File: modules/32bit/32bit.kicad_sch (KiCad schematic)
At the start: 62 parts, among them J5 USB_C_Receptacle_USB2.0_14P, SW1 K2-1808SN-A4SW-01, SW2 K2-1808SN-A4SW-01, SW4 K2-1808SN-A4SW-01, U1 ESP32-S3-WROOM-1U-N16R8, U3 MCP6002-xSN

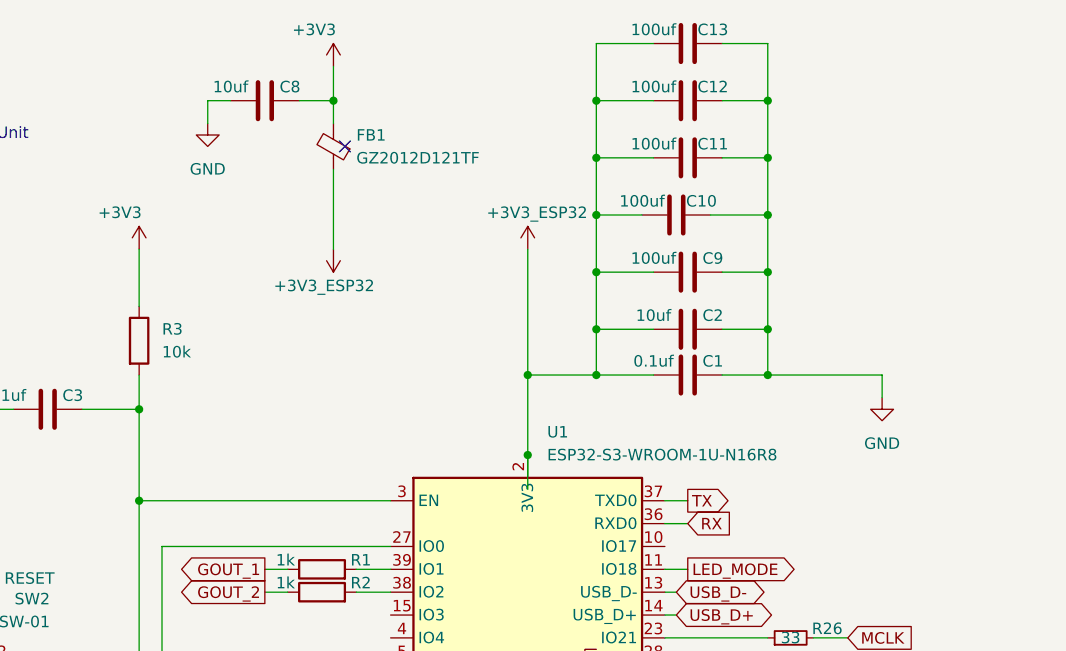
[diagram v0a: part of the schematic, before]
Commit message: Remove 32bit unwanted caps & etc
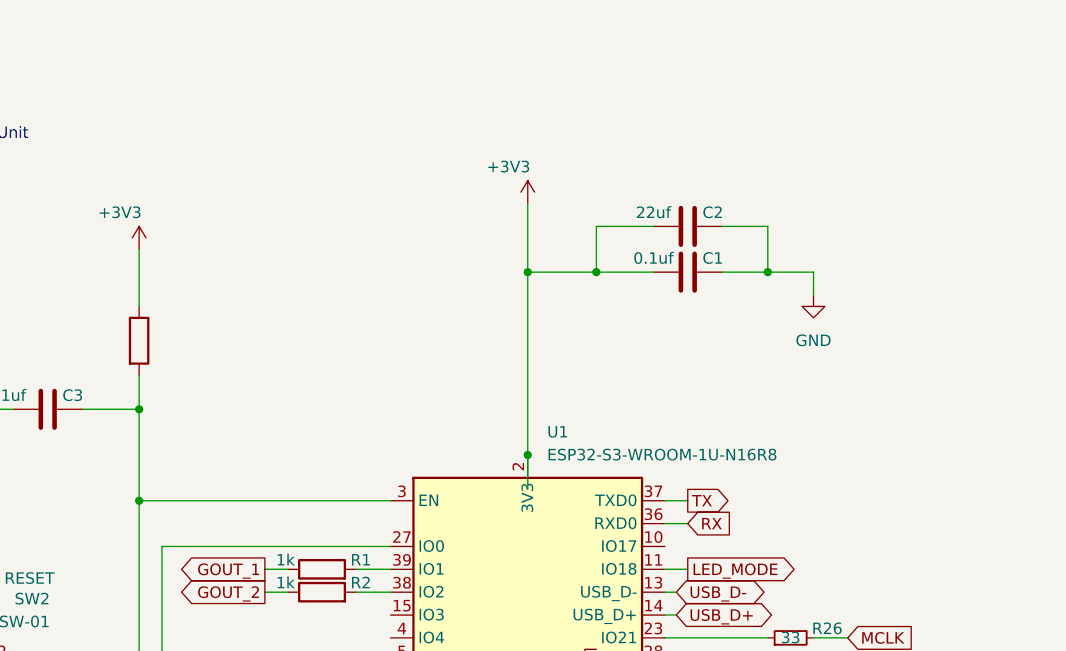
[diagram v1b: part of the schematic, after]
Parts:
- removed C10, C11, C12, C13, C9: 100uf, Capacitor_SMD:C_1206_3216Metric, symbol Device:C
- removed C8: 10uf, Capacitor_SMD:C_0603_1608Metric, symbol Device:C
- removed FB1: GZ2012D121TF, Capacitor_SMD:C_0805_2012Metric, symbol Device:FerriteBead_Small
- C2: value 10uf -> 22uf
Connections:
- net +3V3_ESP32 is gone; now on net +3V3: C1.1, C2.1, U1.2 (3V3)
- no-connect marks 1 -> 0
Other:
- moved on the sheet: C1, C2

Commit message: Add two LDO approach
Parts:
- removed C7: 100uf, Capacitor_SMD:C_1206_3216Metric, symbol Device:C_Small
- removed R15: 10, Resistor_SMD:R_0603_1608Metric, symbol Device:R_Small
- added C10, C7: 10uf, Capacitor_SMD:C_1206_3216Metric, symbol Device:C
- added C12: 100uf, Capacitor_SMD:C_1206_3216Metric, symbol Device:C
- added C17, C8: 22uf, Capacitor_SMD:C_1206_3216Metric, symbol Device:C
- added C9: 0.1uf, Capacitor_SMD:C_0402_1005Metric, symbol Device:C
- added FB1: GZ2012E800TF, Capacitor_SMD:C_0805_2012Metric, symbol Device:FerriteBead_Small
- added U5: AP2112K-3.3, Package_TO_SOT_SMD:SOT-23-5, symbol Regulator_Linear:AP2112K-3.3
- added U6: LP5907MFX-3.3, Package_TO_SOT_SMD:SOT-23-5, symbol Regulator_Linear:LP5907MFX-3.3
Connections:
- net +3V3: no longer C1.1, C2.1, C6.1, R10.1, R12.1, R3.1, U1.2 (3V3), U3.8 (V+)
- net +3V3_8388: no longer C21.1, C26.1, C37.1, C38.1, C39.1, C5.1, U4.16 (HPVDD), U4.17 (AVDD), U4.2 (DVDD)
- net GND: now also C17.2, C9.2
- net at J5.A4 (VBUS), J5.A9 (VBUS), J5.B4 (VBUS)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: now also C17.1, C9.1, FB1.1
- new net: C10.2, C7.2, U6.2 (GND)
- new net: C12.2, C8.2, U5.2 (GND)
- new net +3V3_ANALOG: C10.1, C26.1, C37.1, C38.1, C39.1, C6.1, R10.1, R12.1, U3.8 (V+), U4.16 (HPVDD), U4.17 (AVDD), U6.5 (OUT)
- new net +3V3_DIGITAL: C1.1, C12.1, C2.1, C21.1, C5.1, R3.1, U1.2 (3V3), U4.2 (DVDD), U5.5 (VOUT)
- new net +5V: C7.1, C8.1, FB1.2, U5.1 (VIN), U5.3 (EN), U6.1 (IN), U6.3 (EN)
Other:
- note added: "## 3.3V Analog"
- note added: "## 3.3V Digital"

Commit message: Add the routing
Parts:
- removed C17: 22uf, Capacitor_SMD:C_1206_3216Metric, symbol Device:C
- removed C7: 10uf, Capacitor_SMD:C_1206_3216Metric, symbol Device:C
- added C11, C7: 10uf, Capacitor_SMD:C_0402_1005Metric, symbol Device:C_Small
- C10: value 10uf -> 22uf; footprint Capacitor_SMD:C_1206_3216Metric -> Capacitor_SMD:C_0603_1608Metric
- C8: footprint Capacitor_SMD:C_1206_3216Metric -> Capacitor_SMD:C_0603_1608Metric
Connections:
- net +3V3_8388 is gone; now on net +3V3_DIGITAL: C22.1, R24.2, R25.2, U4.3 (PVDD)
- net +3V3_ANALOG: now also C11.2; no longer C10.1
- net +5V: now also C10.2, C7.2; no longer C8.1
- net GND: now also C10.1, C12.2, C8.1, U5.2 (GND), U6.2 (GND), C11.1, C7.1
- net at C9.1, FB1.1, J5.A4 (VBUS)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: now also C8.2
